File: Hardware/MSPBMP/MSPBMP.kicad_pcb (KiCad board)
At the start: 2 copper layers, 73.7 x 38.1 mm, 49 parts, among them J1 USB_B_Micro, J2 SWD, J3 RS232, J4 JTAG, J5 ISP, U1 MCP1700T-3302E/TT, U2 STM32F103CBT6, U3 LM358DR2G, U4 TXS0108EPWR, Y1 8MHz

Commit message: Schematics and PCB review
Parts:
- added C22: 100nF, Capacitor_SMD:C_0603_1608Metric_Pad1.08x0.95mm_HandSolder, F.Cu at (130.6, 64.8)
- added R15: 47K, Resistor_SMD:R_0603_1608Metric_Pad0.98x0.95mm_HandSolder, F.Cu at (117.9, 77.1)
- U1: value MCP1700T-3302E/TT -> AMS1117-3.3; footprint Package_TO_SOT_SMD:SOT-23 -> Package_TO_SOT_SMD:SOT-223-3_TabPin2
- moved C5 5.02 mm to (86.0, 63.9)
- moved C4 5.02 mm to (84.4, 63.9)
- moved U1 4.06 mm to (79.0, 62.0)
- moved C19 3.47 mm to (92.4, 60.5)
- moved C21 3.47 mm to (94.1, 60.5)
- moved C20 0.63 mm to (130.6, 62.2)
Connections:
- C20 pad 1: /VCC_TOOL -> +3V3
- J4 pad 2: /VCC_TOOL -> +3V3
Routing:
- net +3V3: track 144.9 -> 167.5 mm
- net /VCC_TOOL: track 44.6 -> 30.3 mm
- net /TVCC: track 34.3 -> 39.5 mm
- net /JENA: track 15.9 -> 17.7 mm
- net /JTDO: track 23.8 -> 24.8 mm
- net GND: vias 33 -> 32
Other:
- board text added: "3v3"
- board text added: "V2"
- board text removed: "Tool"
- board text removed: "VCC"

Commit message: More Hardware improvements
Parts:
- removed the R6 at (113.4, 85.5)
- removed the U3 at (99.8, 58.8)
- added NT1: 0, NetTie:NetTie-2_SMD_Pad0.5mm, F.Cu at (105.8, 63.8)
- added RN1: 33, Resistor_SMD:R_Array_Convex_4x0402, F.Cu at (104.3, 69.8)
- added RN2: 33, Resistor_SMD:R_Array_Convex_4x0402, F.Cu at (117.2, 74.4)
- added RN3: 33, Resistor_SMD:R_Array_Convex_4x0402, F.Cu at (117.2, 77.2)
- added U4: LM358DR2G, Package_SO:SOIC-8_3.9x4.9mm_P1.27mm, F.Cu at (110.7, 83.0)
- C12: renamed from C10; value 4.7uF -> 22uF
- C16: renamed from C14; value 4.7uF -> 22uF
- C19: renamed from C18; value 4.7uF -> 22uF
- C2: value 4.7uF -> 10uF
- C20: renamed from C19; value 4.7uF -> 22uF
- C4: value 4.7uF -> 22uF
- C6: value 100nF -> 470nF
- J1: footprint Connector_USB:USB_Mini-B_Lumberg_2486_01_Horizontal -> lib:USB_Mini-B_Lumberg_2486_01_Horizontal_hand_soldered
- moved C11 28.2 mm to (105.1, 54.6), turned to 180 degrees
- moved Y1 27.2 mm to (101.7, 57.5), turned to 0 degrees
- moved R8 26.8 mm to (106.0, 57.2), turned to 270 degrees
- moved R11 26.3 mm to (103.3, 60.2), turned to 180 degrees
- moved C13 25.2 mm to (103.3, 61.8), turned to 180 degrees
- moved C7 25.0 mm to (109.3, 55.5), turned to 0 degrees
- moved C20 24.9 mm to (101.0, 83.8)
- moved C21 24.9 mm to (102.7, 83.8)
- moved C18 24.5 mm to (116.8, 80.7)
- moved C19 24.5 mm to (116.8, 82.4)
- moved C9 23.9 mm to (97.5, 57.4), turned to 90 degrees
- moved R9 22.8 mm to (112.8, 55.5), turned to 0 degrees
- moved R7 22.4 mm to (104.5, 66.5), turned to 270 degrees
- moved C6 19.0 mm to (106.0, 66.5), turned to 270 degrees
- moved R12 17.8 mm to (130.6, 63.1)
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- renumbered C9 to C10, C12 to C11, C22 to C14, C16 to C17, C17 to C18, C20 to C22, C11 to C9, R13 to R10, R14 to R11, R11 to R12, R8 to R13, R12 to R14, R7 to R5, R15 to R6, R5 to R7, R9 to R8, R10 to R9, U4 to U3
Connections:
- J3 pad 1: /TRXD -> Net-(J3-Pad1)
- J3 pad 3: /TTXD -> Net-(J3-Pad3)
- J5 pad 4: +5V -> +3V3
- U3 pad 12: /TRXD -> /BRXD
- U3 pad 13: /TTXD -> /BTXD
- U3 pad 14: /TRST -> Net-(RN3-Pad2)
- U3 pad 15: /TTEST -> Net-(RN3-Pad1)
- U3 pad 16: /TTCK -> Net-(RN2-Pad4)
- U3 pad 17: /TTMS -> Net-(RN2-Pad3)
- U3 pad 18: /TTDI -> Net-(RN2-Pad2)
- U3 pad 20: /TTDO -> Net-(RN2-Pad1)
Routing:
- net /TRXD: track 33.6 -> 7.47 mm, vias 1 -> 0
- net /TTXD: track 32.9 -> 7.82 mm, vias 2 -> 0
- net +5V: track 48.8 -> 73.8 mm, vias 0 -> 3
- net /BRXD: track 0.00 -> 22.6 mm, vias 0 -> 2
- net /BTXD: track 0.00 -> 20.7 mm, vias 0 -> 2
- net /JTDO: track 24.8 -> 8.09 mm
- net /TRST: track 20.6 -> 5.08 mm
- net /TRACESWO: track 18.7 -> 33.2 mm
- net /SWCLK: track 18.8 -> 33.1 mm
- net /USBP: track 32.2 -> 45.6 mm
- net /USBM: track 32.5 -> 44.5 mm
- net /LED_RED: track 43.0 -> 54.5 mm
- net /JRST: track 9.67 -> 20.8 mm, vias 0 -> 2
- net /JTMS: track 20.6 -> 9.82 mm, vias 2 -> 0
- net /VREF2: track 23.1 -> 12.3 mm
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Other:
- board text removed: "5V"

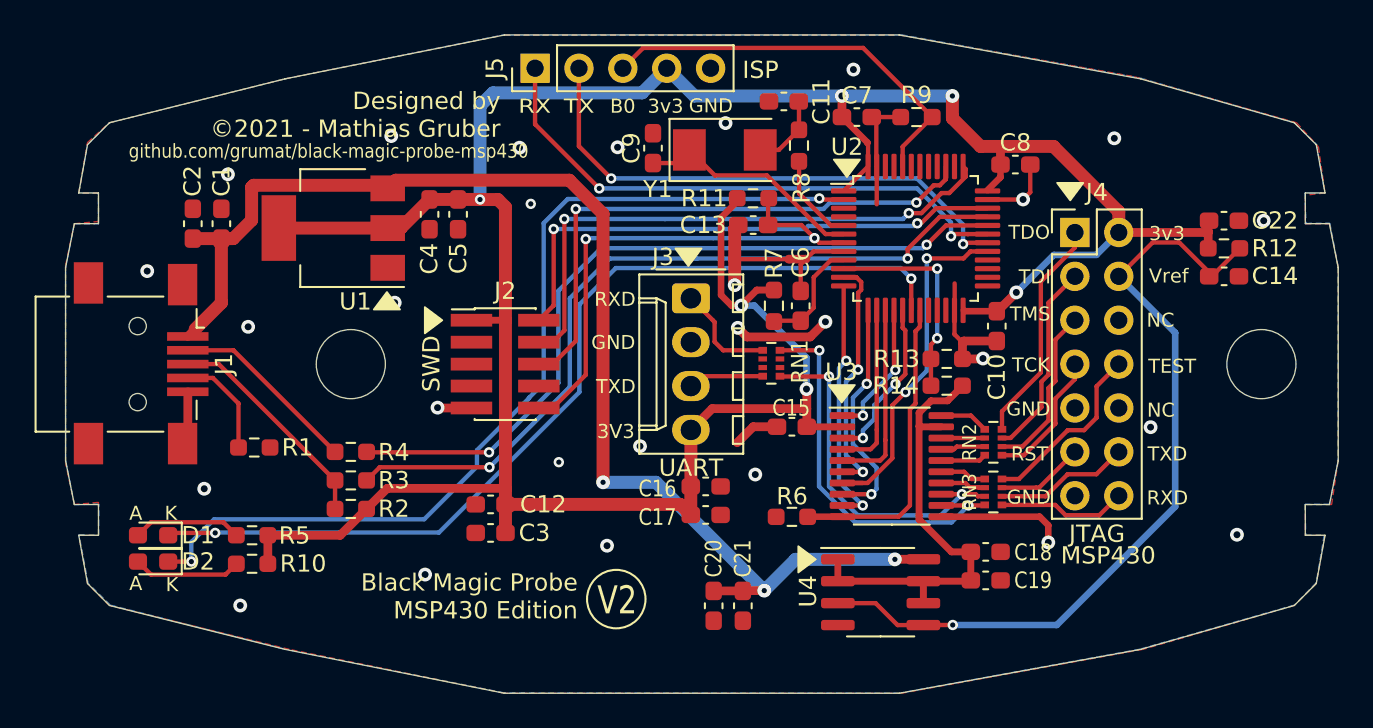
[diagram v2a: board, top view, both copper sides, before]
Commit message: Hardware: New stick version using a newer MCU
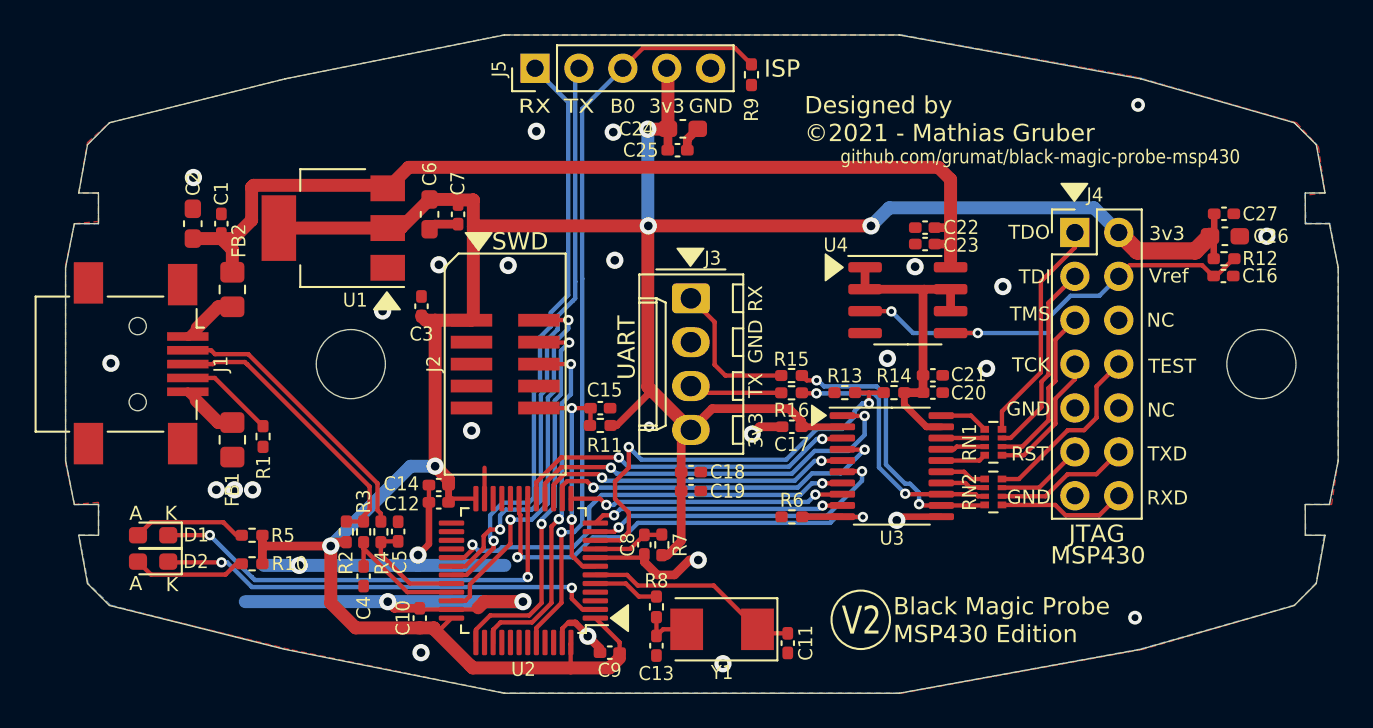
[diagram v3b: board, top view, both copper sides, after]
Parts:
- removed the C9 at (97.5, 57.4)
- removed the RN1 at (104.3, 69.8)
- added C13: 20pF, Capacitor_SMD:C_0402_1005Metric_Pad0.74x0.62mm_HandSolder, F.Cu at (97.7, 86.2)
- added C24: 22uF, Capacitor_SMD:C_0603_1608Metric_Pad1.08x0.95mm_HandSolder, F.Cu at (99.2, 56.2)
- added C25: 100nF, Capacitor_SMD:C_0402_1005Metric_Pad0.74x0.62mm_HandSolder, F.Cu at (98.9, 57.5)
- added C26: 22uF, Capacitor_SMD:C_0603_1608Metric_Pad1.08x0.95mm_HandSolder, F.Cu at (130.6, 62.5)
- added C4: 20pF, Capacitor_SMD:C_0402_1005Metric_Pad0.74x0.62mm_HandSolder, F.Cu at (80.8, 82.1)
- added C5: 20pF, Capacitor_SMD:C_0402_1005Metric_Pad0.74x0.62mm_HandSolder, F.Cu at (82.8, 79.5)
- added FB1: 600, Resistor_SMD:R_0805_2012Metric_Pad1.20x1.40mm_HandSolder, F.Cu at (73.2, 74.2)
- added FB2: 600, Resistor_SMD:R_0805_2012Metric_Pad1.20x1.40mm_HandSolder, F.Cu at (73.2, 65.5)
- added R15: 330, Resistor_SMD:R_0402_1005Metric_Pad0.72x0.64mm_HandSolder, F.Cu at (105.5, 70.5)
- added R16: 330, Resistor_SMD:R_0402_1005Metric_Pad0.72x0.64mm_HandSolder, F.Cu at (105.5, 71.5)
- C1, C11, C3: footprint Capacitor_SMD:C_0603_1608Metric_Pad1.08x0.95mm_HandSolder -> Capacitor_SMD:C_0402_1005Metric_Pad0.74x0.62mm_HandSolder
- C10: renamed from C8; footprint Capacitor_SMD:C_0603_1608Metric_Pad1.08x0.95mm_HandSolder -> Capacitor_SMD:C_0402_1005Metric_Pad0.74x0.62mm_HandSolder
- C12: renamed from C10; footprint Capacitor_SMD:C_0603_1608Metric_Pad1.08x0.95mm_HandSolder -> Capacitor_SMD:C_0402_1005Metric_Pad0.74x0.62mm_HandSolder
- C14: renamed from C12; value 22uF -> 10uF; footprint Capacitor_SMD:C_0603_1608Metric_Pad1.08x0.95mm_HandSolder -> Capacitor_SMD:C_0402_1005Metric_Pad0.74x0.62mm_HandSolder
- C15: renamed from C13; footprint Capacitor_SMD:C_0603_1608Metric_Pad1.08x0.95mm_HandSolder -> Capacitor_SMD:C_0402_1005Metric_Pad0.74x0.62mm_HandSolder
- C16: renamed from C14; footprint Capacitor_SMD:C_0603_1608Metric_Pad1.08x0.95mm_HandSolder -> Capacitor_SMD:C_0402_1005Metric_Pad0.74x0.62mm_HandSolder
- C17: renamed from C15; footprint Capacitor_SMD:C_0603_1608Metric_Pad1.08x0.95mm_HandSolder -> Capacitor_SMD:C_0402_1005Metric_Pad0.74x0.62mm_HandSolder
- C18: renamed from C16; value 22uF -> 10uF; footprint Capacitor_SMD:C_0603_1608Metric_Pad1.08x0.95mm_HandSolder -> Capacitor_SMD:C_0402_1005Metric_Pad0.74x0.62mm_HandSolder
- C19: renamed from C17; footprint Capacitor_SMD:C_0603_1608Metric_Pad1.08x0.95mm_HandSolder -> Capacitor_SMD:C_0402_1005Metric_Pad0.74x0.62mm_HandSolder
- C20: renamed from C18; footprint Capacitor_SMD:C_0603_1608Metric_Pad1.08x0.95mm_HandSolder -> Capacitor_SMD:C_0402_1005Metric_Pad0.74x0.62mm_HandSolder
- C21: renamed from C19; value 22uF -> 10uF; footprint Capacitor_SMD:C_0603_1608Metric_Pad1.08x0.95mm_HandSolder -> Capacitor_SMD:C_0402_1005Metric_Pad0.74x0.62mm_HandSolder
- C22: renamed from C20; value 22uF -> 10uF; footprint Capacitor_SMD:C_0603_1608Metric_Pad1.08x0.95mm_HandSolder -> Capacitor_SMD:C_0402_1005Metric_Pad0.74x0.62mm_HandSolder
- C23: renamed from C21; footprint Capacitor_SMD:C_0603_1608Metric_Pad1.08x0.95mm_HandSolder -> Capacitor_SMD:C_0402_1005Metric_Pad0.74x0.62mm_HandSolder
- C27: renamed from C22; footprint Capacitor_SMD:C_0603_1608Metric_Pad1.08x0.95mm_HandSolder -> Capacitor_SMD:C_0402_1005Metric_Pad0.74x0.62mm_HandSolder
- C7: renamed from C5; footprint Capacitor_SMD:C_0603_1608Metric_Pad1.08x0.95mm_HandSolder -> Capacitor_SMD:C_0402_1005Metric_Pad0.74x0.62mm_HandSolder
- C8: renamed from C6; footprint Capacitor_SMD:C_0603_1608Metric_Pad1.08x0.95mm_HandSolder -> Capacitor_SMD:C_0402_1005Metric_Pad0.74x0.62mm_HandSolder
- C9: renamed from C7; footprint Capacitor_SMD:C_0603_1608Metric_Pad1.08x0.95mm_HandSolder -> Capacitor_SMD:C_0402_1005Metric_Pad0.74x0.62mm_HandSolder
- J2: footprint Connector_PinHeader_1.27mm:PinHeader_2x05_P1.27mm_Vertical_SMD -> lib:PinHeader_2x05_P1.27mm_Vertical_SMD_case
- R1, R10, R11, R12, R13, R14, R2, R3, R4, R5, R6, R7, R8, R9: footprint Resistor_SMD:R_0603_1608Metric_Pad0.98x0.95mm_HandSolder -> Resistor_SMD:R_0402_1005Metric_Pad0.72x0.64mm_HandSolder
- moved C10 43.3 mm to (84.0, 84.5), turned to 90 degrees
- moved C9 34.1 mm to (95.0, 86.5), turned to 180 degrees
- moved C12 33.9 mm to (85.1, 77.8), turned to 180 degrees
- moved C11 31.4 mm to (105.3, 86.0), turned to 270 degrees
- moved U2 29.7 mm to (90.0, 81.8), turned to 180 degrees
- moved R8 27.9 mm to (97.7, 83.9), turned to 90 degrees
- moved Y1 27.7 mm to (101.5, 85.2), turned to 180 degrees
- moved C22 25.1 mm to (113.2, 62.0), turned to 180 degrees
- moved C23 23.4 mm to (113.2, 62.9), turned to 0 degrees
- moved NT1 19.8 mm to (98.2, 82.0), turned to 0 degrees
- moved U4 17.0 mm to (112.2, 66.2)
- moved C8 16.5 mm to (97.0, 80.3), turned to 90 degrees
- moved R11 15.8 mm to (94.5, 73.4), turned to 0 degrees
- moved R7 15.3 mm to (98.0, 80.3), turned to 90 degrees
- moved C15 13.8 mm to (94.5, 72.4), turned to 0 degrees
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- renumbered C4 to C6, RN2 to RN1, RN3 to RN2
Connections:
- net /USBM renamed /USB-
- net /USBP renamed /USB+
- net Net-(J1-Pad2) renamed /E_USB-
- net Net-(J1-Pad3) renamed /E_USB+
- C11 pad 1: Net-(C11-Pad1) -> /OSC_OUT
- J1 pad 1: +5V -> Net-(FB2-Pad2)
- J1 pad 5: GND -> Net-(FB1-Pad1)
- R8 pad 1: Net-(C11-Pad1) -> Net-(C13-Pad1)
- Y1 pad 2: Net-(C11-Pad1) -> Net-(C13-Pad1)
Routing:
- net /USB-: track 44.5 -> 6.52 mm, vias 2 -> 0
- net /USB+: track 45.6 -> 7.90 mm, vias 2 -> 0
- net /LED_RED: track 54.5 -> 26.3 mm
- net /LED_GREEN: track 54.5 -> 26.5 mm
- net /TVCC: track 47.0 -> 26.3 mm, vias 1 -> 2
- net /BOOT0: track 23.6 -> 44.1 mm, vias 0 -> 1
- net +5V: track 73.8 -> 56.0 mm, vias 3 -> 0
- net /NRST: track 31.0 -> 15.0 mm
- net /JTDO: track 8.09 -> 23.3 mm
- net /VREF2: track 12.3 -> 25.7 mm
- net GND: track 46.7 -> 59.3 mm, vias 28 -> 30
- net /TRACESWO: track 33.2 -> 20.9 mm
- net /JTMS: track 9.82 -> 20.7 mm, vias 0 -> 2
- net /SWCLK: track 33.1 -> 22.7 mm
- net /JTDI: track 10.1 -> 20.2 mm
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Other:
- net class Analog: clearance 0.254 -> 0.2
- net class Diff added: clearance 0.2, trace_width 0.254, via_dia 0.6, via_drill 0.3
- board text removed: "3V3"

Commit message: Version 2 of Normal PCB
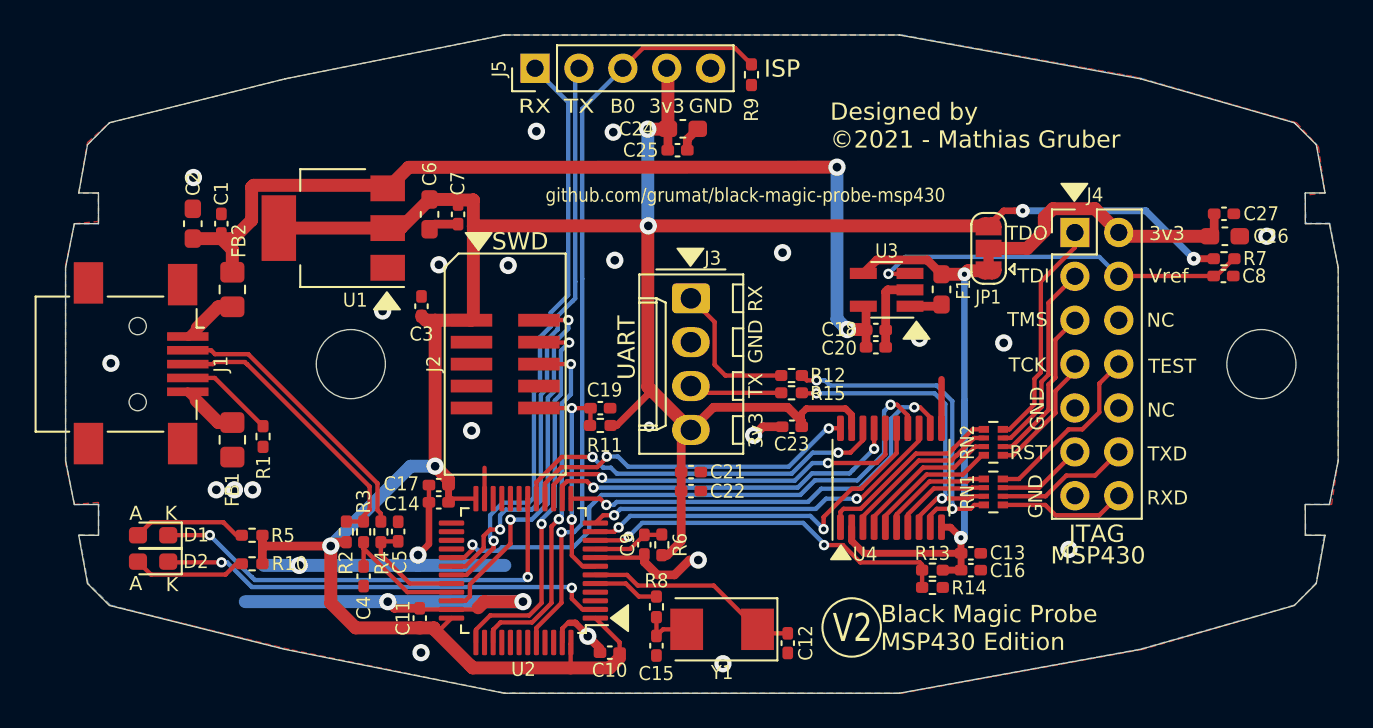
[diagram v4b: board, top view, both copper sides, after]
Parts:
- removed the R6 at (105.5, 78.7)
- removed the U4 at (112.2, 66.2)
- added F1: Polyfuse, Fuse:Fuse_0603_1608Metric_Pad1.05x0.95mm_HandSolder, F.Cu at (114.2, 65.5)
- added JP1: VCC_SEL, Jumper:SolderJumper-3_P1.3mm_Bridged12_RoundedPad1.0x1.5mm, F.Cu at (116.9, 63.1)
- added U3: AD8531ARTZ, Package_TO_SOT_SMD:SOT-23-5_HandSoldering, F.Cu at (111.0, 65.5)
- RN1: renamed from RN2; footprint Resistor_SMD:R_Array_Convex_4x0402 -> lib:R_Array_Convex_4x0402_hand_soldered
- RN2: renamed from RN1; footprint Resistor_SMD:R_Array_Convex_4x0402 -> lib:R_Array_Convex_4x0402_hand_soldered
- moved R14 12.4 mm to (113.7, 82.8), turned to 0 degrees
- moved C16 11.5 mm to (115.9, 81.8)
- moved R13 10.5 mm to (113.7, 81.8)
- moved C13 9.56 mm to (115.9, 80.8)
- moved C20 6.62 mm to (110.4, 68.9), turned to 180 degrees
- moved C18 6.57 mm to (110.4, 67.9), turned to 0 degrees
- moved U4 0.67 mm to (111.3, 76.4), turned to 90 degrees
- turned C23 to 0 degrees
- renumbered C9 to C10, C10 to C11, C11 to C12, C20 to C13, C12 to C14, C13 to C15, C21 to C16, C14 to C17, C22 to C18, C15 to C19, C23 to C20, C18 to C21, C19 to C22, C17 to C23, C16 to C8, C8 to C9, R15 to R12, R14 to R13, R13 to R14, R16 to R15, R7 to R6, R12 to R7, U3 to U4
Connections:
- C23 pad 1: +3V3 -> GND
- C23 pad 2: GND -> +3V3
- C26 pad 2: +3V3 -> /VCC_OUT
- C27 pad 1: +3V3 -> /VCC_OUT
- J4 pad 2: +3V3 -> /VCC_OUT
- R12 pad 2: /BRXD -> /LRXD
- R15 pad 2: /BTXD -> /LTXD
- RN1 pad 1: Net-(RN2-Pad1) -> /LTEST
- RN1 pad 2: Net-(RN2-Pad2) -> /LRST
- RN1 pad 3: /BTXD -> /LTXD
- RN1 pad 4: /BRXD -> /LRXD
- RN2 pad 1: Net-(RN1-Pad1) -> /LTDO
- RN2 pad 2: Net-(RN1-Pad2) -> /LTDI
- RN2 pad 3: Net-(RN1-Pad3) -> /LTMS
- RN2 pad 4: Net-(RN1-Pad4) -> /LTCK
- U2 pad 19: /JENA -> Net-(U2-Pad19)
- U4 pad 1: /JTDO -> /LTDO
- U4 pad 10: /JENA -> /VCC_TOOL
- U4 pad 12: /BRXD -> /JRXD
- U4 pad 13: /BTXD -> /JTXD
- U4 pad 14: Net-(RN2-Pad2) -> /JRST
- U4 pad 15: Net-(RN2-Pad1) -> /JTEST
- U4 pad 16: Net-(RN1-Pad4) -> /JTCK
- U4 pad 17: Net-(RN1-Pad3) -> /JTMS
- U4 pad 18: Net-(RN1-Pad2) -> /JTDI
- U4 pad 19: /VCC_TOOL -> +3V3
- U4 pad 2: +3V3 -> /VCC_TOOL
- U4 pad 20: Net-(RN1-Pad1) -> /JTDO
- U4 pad 3: /JTDI -> /LTDI
- U4 pad 4: /JTMS -> /LTMS
- U4 pad 5: /JTCK -> /LTCK
- U4 pad 6: /JTEST -> /LTEST
- U4 pad 7: /JRST -> /LRST
- U4 pad 8: /JRXD -> /LTXD
- U4 pad 9: /JTXD -> /LRXD
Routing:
- net /JENA: track 27.7 -> 0.00 mm, vias 2 -> 0
- net /LRXD: track 0.00 -> 19.6 mm, vias 0 -> 2
- net /LTXD: track 0.00 -> 19.0 mm, vias 0 -> 2
- net /VCC_TOOL: track 17.9 -> 35.1 mm, vias 0 -> 2
- net /BRXD: track 16.4 -> 0.00 mm, vias 2 -> 0
- net /VCC_OUT: track 0.00 -> 16.3 mm
- net /BTXD: track 15.4 -> 0.00 mm, vias 2 -> 0
- net /LTDO: track 0.00 -> 11.2 mm
- net /LTDI: track 0.00 -> 9.50 mm
- net /JRXD: track 16.1 -> 25.4 mm
- net /LTMS: track 0.00 -> 8.64 mm
- net /JRST: track 25.7 -> 33.8 mm
- net /LTCK: track 0.00 -> 7.81 mm
- net /JTXD: track 14.7 -> 21.5 mm
- net /LTEST: track 0.00 -> 6.64 mm
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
